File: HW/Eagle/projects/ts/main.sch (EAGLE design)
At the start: 48 parts, among them IC1 4050D, Q1 20 MHz, T1 IRFZ24N, T2 IRFZ24N, U1 ATMEGA328P-PU, U2 LM2576T, U3 HT7533, U4 LM75

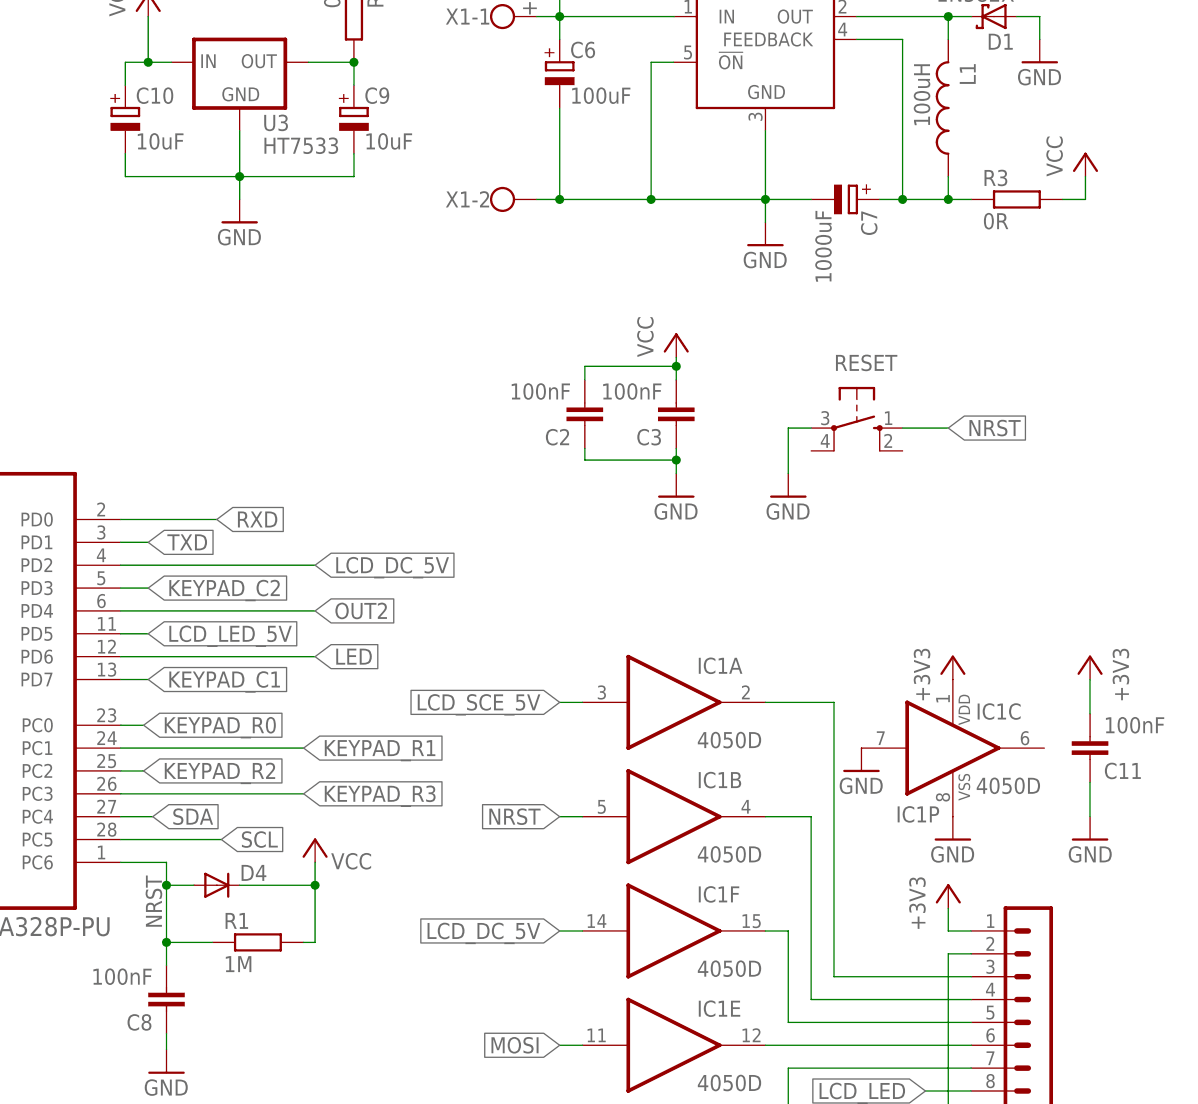
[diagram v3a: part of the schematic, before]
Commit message: [HW] Removed some parts, updated layout
Removed unessential parts (0 Ohm resistor, reset pin protection diode).
Optimized layout to optimize some connections.
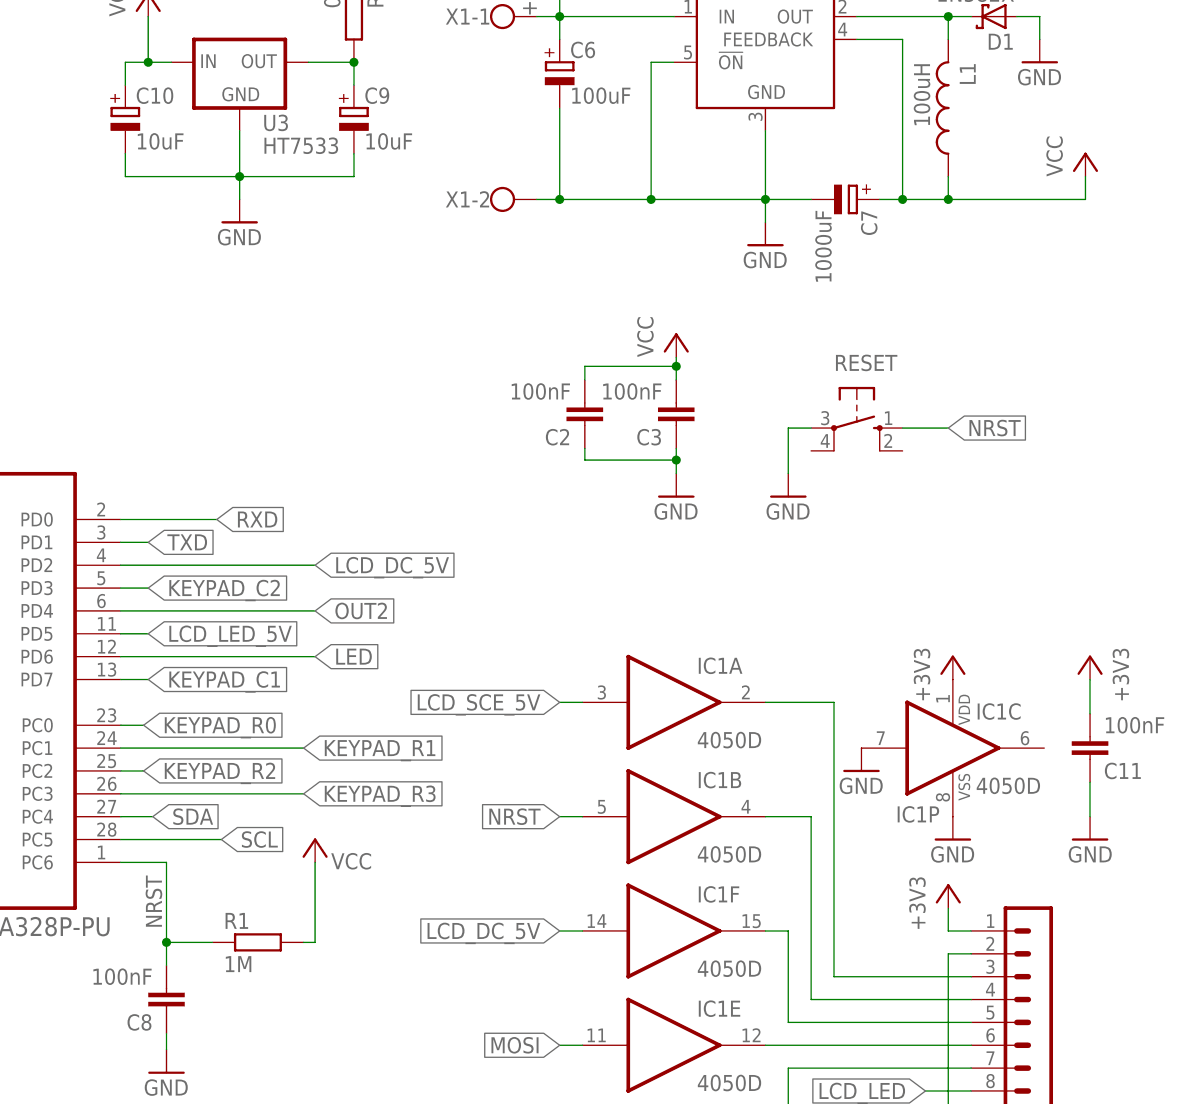
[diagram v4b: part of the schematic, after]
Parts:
- removed D4: (no value), diode:DIODE-MINIMELF
- removed R3: 0R, rcl:R-EU_R0805
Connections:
- net N$10 renamed OUT1_OC
- net N$11 renamed OUT2_OC
- net N$7 renamed OUT_5V
- removed net N$8: C7.+, L1.1, R3.1, U2.FEEDBACK
- net NRST: no longer D4.A
- net VCC: now also C7.+, L1.1, U2.FEEDBACK; no longer D4.C, R3.2
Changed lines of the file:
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@@
 <part name="C7" library="rcl" deviceset="CPOL-EU" device="TT5D10" value="1000uF"/>
 <part name="L1" library="rcl" deviceset="L-US" device="TJ3-U1" value="100uH"/>
-<part name="R3" library="rcl" deviceset="R-EU_" device="R0805" value="0R"/>
 <part name="P+6" library="supply1" deviceset="VCC" device=""/>
 <part name="X1" library="con-wago-500" deviceset="W237-102" device=""/>
@@
 <part name="P+11" library="supply1" deviceset="+12V" device=""/>
 <part name="P+12" library="supply1" deviceset="+12V" device=""/>
-<part name="D4" library="diode" deviceset="DIODE-" device="MINIMELF"/>
 <part name="R12" library="rcl" deviceset="R-EU_" device="R0805" value="330R"/>
 <part name="R13" library="rcl" deviceset="R-EU_" device="R0805" value="330R"/>
@@
 <instance part="C7" gate="G$1" x="220.98" y="139.7" rot="R270"/>
 <instance part="L1" gate="G$1" x="231.14" y="149.86" rot="R180"/>
-<instance part="R3" gate="G$1" x="238.76" y="139.7"/>
 <instance part="P+6" gate="VCC" x="246.38" y="144.78"/>
 <instance part="X1" gate="-1" x="180.34" y="160.02"/>
@@
 <attribute name="VALUE" x="53.34" y="119.38" size="1.778" layer="96"/>
 </instance>
-<instance part="D4" gate="G$1" x="149.86" y="63.5"/>
 <instance part="R12" gate="G$1" x="20.828" y="101.6" rot="R180"/>
 <instance part="R13" gate="G$1" x="20.828" y="121.92" rot="R180"/>
@@
 </segment>
 <segment>
-<pinref part="R3" gate="G$1" pin="2"/>
-<wire x1="243.84" y1="139.7" x2="246.38" y2="139.7" width="0.1524" layer="91"/>
 <pinref part="P+6" gate="VCC" pin="VCC"/>
 <wire x1="246.38" y1="139.7" x2="246.38" y2="142.24" width="0.1524" layer="91"/>
+<pinref part="U2" gate="U" pin="FEEDBACK"/>
+<wire x1="226.06" y1="139.7" x2="226.06" y2="157.48" width="0.1524" layer="91"/>
+<wire x1="226.06" y1="157.48" x2="220.98" y2="157.48" width="0.1524" layer="91"/>
+<pinref part="C7" gate="G$1" pin="+"/>
+<wire x1="223.52" y1="139.7" x2="226.06" y2="139.7" width="0.1524" layer="91"/>
+<pinref part="L1" gate="G$1" pin="1"/>
+<wire x1="231.14" y1="142.24" x2="231.14" y2="139.7" width="0.1524" layer="91"/>
+<wire x1="231.14" y1="139.7" x2="226.06" y2="139.7" width="0.1524" layer="91"/>
+<junction x="226.06" y="139.7"/>
+<junction x="231.14" y="139.7"/>
+<wire x1="246.38" y1="139.7" x2="231.14" y2="139.7" width="0.1524" layer="91"/>
 </segment>
 <segment>
@@
 <pinref part="P+3" gate="VCC" pin="VCC"/>
 <wire x1="159.512" y1="57.15" x2="160.782" y2="57.15" width="0.1524" layer="91"/>
-<wire x1="160.782" y1="57.15" x2="160.782" y2="63.5" width="0.1524" layer="91"/>
-<pinref part="D4" gate="G$1" pin="C"/>
-<wire x1="160.782" y1="63.5" x2="160.782" y2="66.04" width="0.1524" layer="91"/>
-<wire x1="152.4" y1="63.5" x2="160.782" y2="63.5" width="0.1524" layer="91"/>
-<junction x="160.782" y="63.5"/>
+<wire x1="160.782" y1="57.15" x2="160.782" y2="66.04" width="0.1524" layer="91"/>
 </segment>
 <segment>
@@
 <pinref part="R1" gate="G$1" pin="1"/>
 <wire x1="149.352" y1="57.15" x2="144.272" y2="57.15" width="0.1524" layer="91"/>
-<wire x1="144.272" y1="57.15" x2="144.272" y2="63.5" width="0.1524" layer="91"/>
+<wire x1="144.272" y1="57.15" x2="144.272" y2="66.04" width="0.1524" layer="91"/>
 <pinref part="U1" gate="A" pin="PC6"/>
-<wire x1="144.272" y1="63.5" x2="144.272" y2="66.04" width="0.1524" layer="91"/>
 <wire x1="144.272" y1="66.04" x2="139.192" y2="66.04" width="0.1524" layer="91"/>
 <label x="143.764" y="58.674" size="1.778" layer="95" rot="R90"/>
@@
 <wire x1="144.272" y1="57.15" x2="144.272" y2="54.61" width="0.1524" layer="91"/>
 <junction x="144.272" y="57.15"/>
-<pinref part="D4" gate="G$1" pin="A"/>
-<wire x1="147.32" y1="63.5" x2="144.272" y2="63.5" width="0.1524" layer="91"/>
-<junction x="144.272" y="63.5"/>
 </segment>
 <segment>
@@
 </segment>
 </net>
-<net name="N$7" class="0">
+<net name="OUT_5V" class="0">
 <segment>
 <pinref part="U2" gate="U" pin="OUT"/>
@@
 </segment>
 </net>
-<net name="N$8" class="0">
-<segment>
-<pinref part="U2" gate="U" pin="FEEDBACK"/>
-<wire x1="226.06" y1="139.7" x2="226.06" y2="157.48" width="0.1524" layer="91"/>
-<wire x1="226.06" y1="157.48" x2="220.98" y2="157.48" width="0.1524" layer="91"/>
-<pinref part="C7" gate="G$1" pin="+"/>
-<wire x1="223.52" y1="139.7" x2="226.06" y2="139.7" width="0.1524" layer="91"/>
-<pinref part="L1" gate="G$1" pin="1"/>
-<wire x1="231.14" y1="142.24" x2="231.14" y2="139.7" width="0.1524" layer="91"/>
-<wire x1="231.14" y1="139.7" x2="226.06" y2="139.7" width="0.1524" layer="91"/>
-<junction x="226.06" y="139.7"/>
-<pinref part="R3" gate="G$1" pin="1"/>
-<wire x1="231.14" y1="139.7" x2="233.68" y2="139.7" width="0.1524" layer="91"/>
-<junction x="231.14" y="139.7"/>
-</segment>
-</net>
 <net name="MOSI" class="0">
 <segment>
@@
 </segment>
 </net>
-<net name="N$10" class="0">
+<net name="OUT1_OC" class="0">
 <segment>
 <pinref part="X2" gate="-1" pin="KL"/>
@@
 </segment>
 </net>
-<net name="N$11" class="0">
+<net name="OUT2_OC" class="0">
 <segment>
 <pinref part="X2" gate="-2" pin="KL"/>

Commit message: [HW] Minor change
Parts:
- removed R5: 0R, rcl:R-EU_R0805
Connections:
- removed net N$1: C9.+, R5.2, U3.OUT
- net +3V3: now also C9.+, U3.OUT; no longer R5.1
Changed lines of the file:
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@@
 <part name="+3V3" library="supply1" deviceset="+3V3" device=""/>
 <part name="GND10" library="supply1" deviceset="GND" device=""/>
-<part name="R5" library="rcl" deviceset="R-EU_" device="R0805" value="0R"/>
 <part name="GND12" library="supply1" deviceset="GND" device=""/>
 <part name="C11" library="rcl" deviceset="C-EU" device="C0805" value="100nF"/>
@@
 <instance part="C8" gate="G$1" x="144.272" y="49.53" rot="R180"/>
 <instance part="GND7" gate="1" x="144.272" y="42.672"/>
-<instance part="P+7" gate="VCC" x="142.24" y="162.56"/>
+<instance part="P+7" gate="VCC" x="139.7" y="162.56"/>
 <instance part="GND8" gate="1" x="152.4" y="137.16"/>
-<instance part="+3V1" gate="G$1" x="165.1" y="167.64" smashed="yes">
-<attribute name="VALUE" x="165.1" y="167.64" size="1.778" layer="96"/>
-</instance>
+<instance part="+3V1" gate="G$1" x="165.1" y="162.56"/>
 <instance part="U3" gate="G$1" x="152.4" y="154.94"/>
 <instance part="C9" gate="G$1" x="165.1" y="149.86"/>
@@
 <instance part="+3V3" gate="G$1" x="231.14" y="63.5"/>
 <instance part="GND10" gate="1" x="231.14" y="33.02"/>
-<instance part="R5" gate="G$1" x="165.1" y="160.02" rot="R270"/>
 <instance part="GND12" gate="1" x="85.852" y="102.87"/>
 <instance part="C11" gate="G$1" x="246.888" y="77.47" rot="MR180"/>
@@
 <segment>
 <pinref part="P+7" gate="VCC" pin="VCC"/>
-<wire x1="144.78" y1="154.94" x2="142.24" y2="154.94" width="0.1524" layer="91"/>
-<wire x1="142.24" y1="154.94" x2="142.24" y2="160.02" width="0.1524" layer="91"/>
+<wire x1="144.78" y1="154.94" x2="139.7" y2="154.94" width="0.1524" layer="91"/>
+<wire x1="139.7" y1="154.94" x2="139.7" y2="160.02" width="0.1524" layer="91"/>
 <pinref part="U3" gate="G$1" pin="IN"/>
 <pinref part="C10" gate="G$1" pin="+"/>
 <wire x1="139.7" y1="152.4" x2="139.7" y2="154.94" width="0.1524" layer="91"/>
-<wire x1="139.7" y1="154.94" x2="142.24" y2="154.94" width="0.1524" layer="91"/>
-<junction x="142.24" y="154.94"/>
+<junction x="139.7" y="154.94"/>
 </segment>
 <segment>
@@
 </segment>
 <segment>
-<pinref part="R5" gate="G$1" pin="1"/>
-<pinref part="+3V1" gate="G$1" pin="+3V3"/>
-</segment>
-<segment>
 <pinref part="C11" gate="G$1" pin="2"/>
 <pinref part="+3V4" gate="G$1" pin="+3V3"/>
 <wire x1="246.888" y1="86.36" x2="246.888" y2="82.55" width="0.1524" layer="91"/>
 </segment>
-</net>
-<net name="N$1" class="0">
 <segment>
 <pinref part="U3" gate="G$1" pin="OUT"/>
@@
 <wire x1="165.1" y1="152.4" x2="165.1" y2="154.94" width="0.1524" layer="91"/>
 <wire x1="165.1" y1="154.94" x2="160.02" y2="154.94" width="0.1524" layer="91"/>
-<pinref part="R5" gate="G$1" pin="2"/>
+<pinref part="+3V1" gate="G$1" pin="+3V3"/>
+<wire x1="165.1" y1="154.94" x2="165.1" y2="160.02" width="0.1524" layer="91"/>
 <junction x="165.1" y="154.94"/>
 </segment>

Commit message: [HW] Organized schematics
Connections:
- net AREF renamed N$1
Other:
- note added: "CPU"
- note added: "CPU Accessories"
- note added: "Decoupling"
- note added: "Interface"
- note added: "LCD interface"
- note added: "Misc"
- note added: "Outputs"
- note added: "Power supply"
- note added: "Temperature sensor"
- moved on the sheet: C1, C10, C11, C12, C2, C3, C4, C5, C6, C7, C8, C9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
